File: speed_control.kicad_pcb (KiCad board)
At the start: 2 copper layers, 38.1 x 38.1 mm, 17 parts, among them M1 VAL**, M2 VAL**, M3 VAL**, M4 VAL**, P1 CONN_2, P2 CONN_2, Q1 NPN, SW1 SWITCH_INV, U1 LTC6992_TSOT_32_6

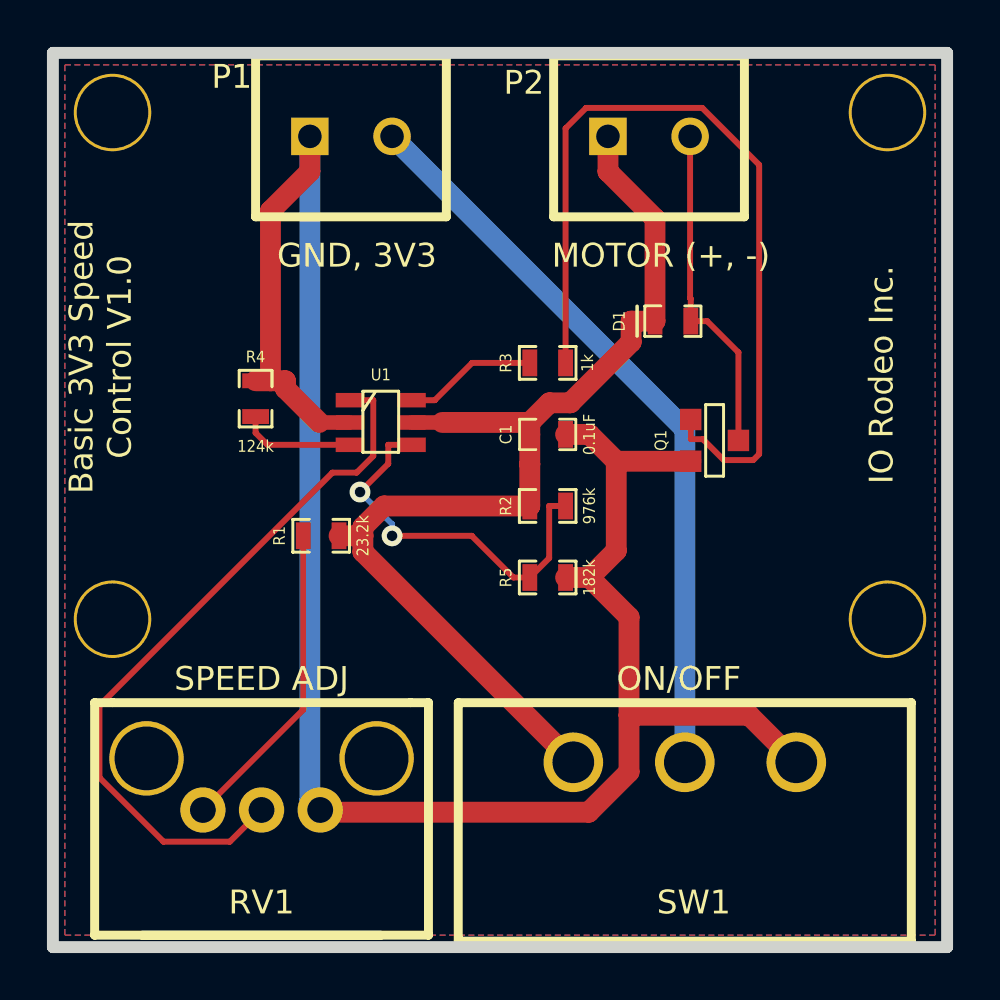
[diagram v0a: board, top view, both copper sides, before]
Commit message: Added trace to PWR class and re-routed. Created gerber files for version 1.1.
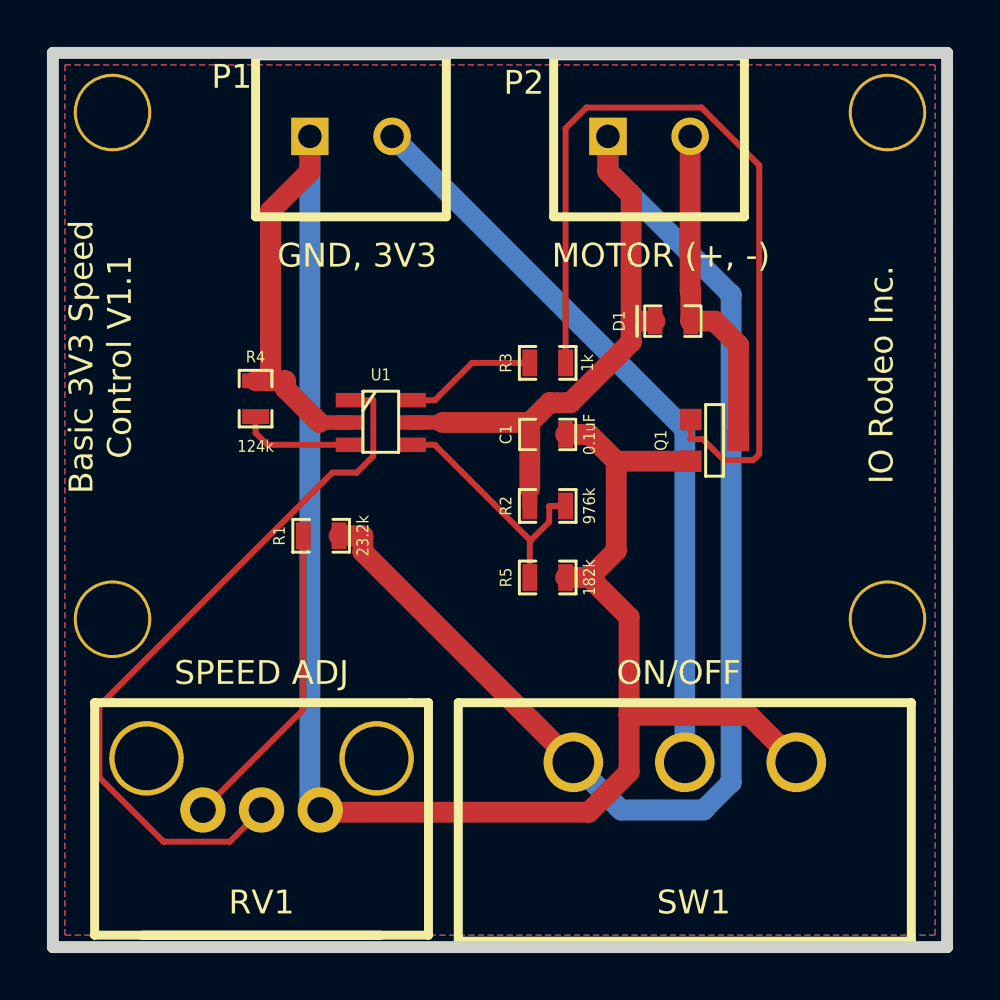
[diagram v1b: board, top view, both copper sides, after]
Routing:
- net +3.3V: track 47.2 -> 76.7 mm
- net N-0000010: track 16.6 -> 10.9 mm, vias 2 -> 0
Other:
- board text added: "Basic 3V3 Speed Control V1.1"
- board text removed: "Basic 3V3 Speed Control V1.0"
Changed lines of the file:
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@@
     (thickness 1.6)
     (drawings 10)
-    (tracks 95)
+    (tracks 90)
     (zones 0)
     (modules 17)
@@
       (drillshape 0)
       (scaleselection 1)
-      (outputdirectory gerber_v1p0/))
+      (outputdirectory gerber_v1p1/))
   )
   (net 0 "")
@@
     (add_net N-000002)
     (add_net N-000003)
-    (add_net N-000004)
     (add_net N-000006)
     (add_net N-000007)
@@
     (add_net GND)
     (add_net N-000001)
+    (add_net N-000004)
   )
   (module SM0603_Capa (layer F.Cu)
@@
     (effects (font (size 1.016 1.016) (thickness 0.2032)))
   )
-  (gr_text "Basic 3V3 Speed \nControl V1.0" (at 27.432 38.354 90) (layer F.SilkS)
+  (gr_text "Basic 3V3 Speed \nControl V1.1" (at 27.432 38.354 90) (layer F.SilkS)
     (effects (font (size 1.016 1.016) (thickness 0.2032)))
   )
-  (gr_text ON/OFF (at 52.07 52.07) (layer F.SilkS)
+  (gr_text ON/OFF (at 52.07 51.816) (layer F.SilkS)
     (effects (font (size 1.016 1.016) (thickness 0.2032)))
   )
-  (gr_text "SPEED ADJ" (at 34.29 52.07) (layer F.SilkS)
+  (gr_text "SPEED ADJ" (at 34.29 51.816) (layer F.SilkS)
     (effects (font (size 1.016 1.016) (thickness 0.2032)))
   )
@@
   (gr_line (start 25.4 63.5) (end 63.5 63.5) (angle 90) (layer Edge.Cuts) (width 0.508))
   (gr_line (start 25.4 25.4) (end 25.4 63.5) (angle 90) (layer Edge.Cuts) (width 0.508))
+  (segment (start 37.592 45.974) (end 38.6083 45.974) (width 0.889) (layer F.Cu) (net 1))
   (segment (start 38.6083 46.6601) (end 38.6083 45.974) (width 0.889) (layer F.Cu) (net 1))
   (segment (start 47.5742 55.626) (end 38.6083 46.6601) (width 0.889) (layer F.Cu) (net 1))
-  (segment (start 37.592 45.974) (end 38.6083 45.974) (width 0.889) (layer F.Cu) (net 1))
-  (segment (start 45.7192 44.704) (end 45.72 44.704) (width 0.6348) (layer F.Cu) (net 1))
-  (segment (start 49.0499 28.956) (end 49.0499 30.4549) (width 0.889) (layer F.Cu) (net 1))
-  (segment (start 39.5078 44.704) (end 45.7192 44.704) (width 0.889) (layer F.Cu) (net 1))
-  (segment (start 38.6083 45.6035) (end 39.5078 44.704) (width 0.889) (layer F.Cu) (net 1))
-  (segment (start 38.6083 45.974) (end 38.6083 45.6035) (width 0.889) (layer F.Cu) (net 1))
-  (segment (start 45.7192 42.9271) (end 45.72 42.9263) (width 0.889) (layer F.Cu) (net 1))
-  (segment (start 45.7192 44.704) (end 45.7192 42.9271) (width 0.889) (layer F.Cu) (net 1))
-  (segment (start 45.72 41.656) (end 45.72 42.9263) (width 0.889) (layer F.Cu) (net 1))
-  (segment (start 51.054 32.459) (end 49.0499 30.4549) (width 0.889) (layer F.Cu) (net 1))
-  (segment (start 51.054 36.83) (end 51.054 32.459) (width 0.889) (layer F.Cu) (net 1))
+  (segment (start 45.72 43.9519) (end 45.72 44.704) (width 0.6348) (layer F.Cu) (net 1))
+  (segment (start 45.72 43.9519) (end 45.72 41.656) (width 0.889) (layer F.Cu) (net 1))
   (segment (start 45.72 41.656) (end 45.72 41.1455) (width 0.889) (layer F.Cu) (net 1))
   (segment (start 41.8567 41.1455) (end 41.8542 41.148) (width 0.6198) (layer F.Cu) (net 1))
   (segment (start 41.989 41.1455) (end 41.8567 41.1455) (width 0.6198) (layer F.Cu) (net 1))
   (segment (start 40.68 41.148) (end 41.8542 41.148) (width 0.6198) (layer F.Cu) (net 1))
+  (segment (start 49.6064 57.6582) (end 47.5742 55.626) (width 0.889) (layer B.Cu) (net 1))
+  (segment (start 53.1243 57.6582) (end 49.6064 57.6582) (width 0.889) (layer B.Cu) (net 1))
+  (segment (start 54.2998 56.4827) (end 53.1243 57.6582) (width 0.889) (layer B.Cu) (net 1))
+  (segment (start 54.2998 35.7048) (end 54.2998 56.4827) (width 0.889) (layer B.Cu) (net 1))
+  (segment (start 49.0499 30.4549) (end 54.2998 35.7048) (width 0.889) (layer B.Cu) (net 1))
+  (segment (start 49.0499 28.956) (end 49.0499 30.4549) (width 0.889) (layer B.Cu) (net 1))
   (segment (start 51.054 36.83) (end 50.0377 36.83) (width 0.889) (layer F.Cu) (net 1))
   (segment (start 45.72 41.1455) (end 41.989 41.1455) (width 0.889) (layer F.Cu) (net 1))
   (segment (start 50.0377 37.7193) (end 50.0377 36.83) (width 0.889) (layer F.Cu) (net 1))
-  (segment (start 47.4476 40.3094) (end 50.0377 37.7193) (width 0.889) (layer F.Cu) (net 1))
-  (segment (start 46.5561 40.3094) (end 47.4476 40.3094) (width 0.889) (layer F.Cu) (net 1))
-  (segment (start 45.72 41.1455) (end 46.5561 40.3094) (width 0.889) (layer F.Cu) (net 1))
+  (segment (start 47.4543 40.3027) (end 50.0377 37.7193) (width 0.889) (layer F.Cu) (net 1))
+  (segment (start 46.5628 40.3027) (end 47.4543 40.3027) (width 0.889) (layer F.Cu) (net 1))
+  (segment (start 45.72 41.1455) (end 46.5628 40.3027) (width 0.889) (layer F.Cu) (net 1))
+  (segment (start 50.0377 31.4427) (end 50.0377 36.83) (width 0.889) (layer F.Cu) (net 1))
+  (segment (start 49.0499 30.4549) (end 50.0377 31.4427) (width 0.889) (layer F.Cu) (net 1))
+  (segment (start 49.0499 28.956) (end 49.0499 30.4549) (width 0.889) (layer F.Cu) (net 1))
   (segment (start 47.244 41.656) (end 48.2603 41.656) (width 0.889) (layer F.Cu) (net 2))
   (segment (start 36.7511 41.148) (end 38.06 41.148) (width 0.6198) (layer F.Cu) (net 2))
@@
   (segment (start 52.324 41.4299) (end 39.8501 28.956) (width 0.889) (layer B.Cu) (net 3))
   (segment (start 52.324 55.626) (end 52.324 41.4299) (width 0.889) (layer B.Cu) (net 3))
-  (via (at 38.4852 44.1096) (size 0.889) (layers F.Cu B.Cu) (net 4))
-  (via (at 39.8521 45.9765) (size 0.889) (layers F.Cu B.Cu) (net 4))
   (segment (start 47.244 44.704) (end 46.5452 44.704) (width 0.254) (layer F.Cu) (net 4))
-  (segment (start 46.5452 46.9268) (end 46.5452 44.704) (width 0.254) (layer F.Cu) (net 4))
-  (segment (start 45.72 47.752) (end 46.5452 46.9268) (width 0.254) (layer F.Cu) (net 4))
-  (segment (start 39.8521 45.4765) (end 38.4852 44.1096) (width 0.254) (layer B.Cu) (net 4))
-  (segment (start 39.8521 45.9765) (end 39.8521 45.4765) (width 0.254) (layer B.Cu) (net 4))
-  (segment (start 39.6887 42.9061) (end 38.4852 44.1096) (width 0.254) (layer F.Cu) (net 4))
-  (segment (start 39.6887 42.098) (end 39.6887 42.9061) (width 0.254) (layer F.Cu) (net 4))
-  (segment (start 43.2457 45.9765) (end 45.0212 47.752) (width 0.254) (layer F.Cu) (net 4))
-  (segment (start 39.8521 45.9765) (end 43.2457 45.9765) (width 0.254) (layer F.Cu) (net 4))
-  (segment (start 45.72 47.752) (end 45.0212 47.752) (width 0.254) (layer F.Cu) (net 4))
-  (segment (start 40.68 42.098) (end 39.6887 42.098) (width 0.254) (layer F.Cu) (net 4))
+  (segment (start 40.68 42.098) (end 41.6713 42.098) (width 0.254) (layer F.Cu) (net 4))
+  (segment (start 41.6713 42.098) (end 45.7521 46.1787) (width 0.254) (layer F.Cu) (net 4))
+  (segment (start 45.72 46.2108) (end 45.7521 46.1787) (width 0.254) (layer F.Cu) (net 4))
+  (segment (start 45.72 47.752) (end 45.72 46.2108) (width 0.254) (layer F.Cu) (net 4))
+  (segment (start 46.5452 45.3856) (end 46.5452 44.704) (width 0.254) (layer F.Cu) (net 4))
+  (segment (start 45.7521 46.1787) (end 46.5452 45.3856) (width 0.254) (layer F.Cu) (net 4))
   (segment (start 53.0975 41.8595) (end 52.578 41.8595) (width 0.254) (layer F.Cu) (net 5))
   (segment (start 53.9866 42.7486) (end 53.0975 41.8595) (width 0.254) (layer F.Cu) (net 5))
-  (segment (start 55.2392 42.7486) (end 53.9866 42.7486) (width 0.254) (layer F.Cu) (net 5))
-  (segment (start 55.492 42.4958) (end 55.2392 42.7486) (width 0.254) (layer F.Cu) (net 5))
-  (segment (start 55.492 30.1687) (end 55.492 42.4958) (width 0.254) (layer F.Cu) (net 5))
-  (segment (start 53.0672 27.7439) (end 55.492 30.1687) (width 0.254) (layer F.Cu) (net 5))
-  (segment (start 48.1173 27.7439) (end 53.0672 27.7439) (width 0.254) (layer F.Cu) (net 5))
-  (segment (start 47.244 28.6172) (end 48.1173 27.7439) (width 0.254) (layer F.Cu) (net 5))
+  (segment (start 55.2434 42.7486) (end 53.9866 42.7486) (width 0.254) (layer F.Cu) (net 5))
+  (segment (start 55.4971 42.4949) (end 55.2434 42.7486) (width 0.254) (layer F.Cu) (net 5))
+  (segment (start 55.4971 30.1916) (end 55.4971 42.4949) (width 0.254) (layer F.Cu) (net 5))
+  (segment (start 53.0324 27.7269) (end 55.4971 30.1916) (width 0.254) (layer F.Cu) (net 5))
+  (segment (start 48.1343 27.7269) (end 53.0324 27.7269) (width 0.254) (layer F.Cu) (net 5))
+  (segment (start 47.244 28.6172) (end 48.1343 27.7269) (width 0.254) (layer F.Cu) (net 5))
   (segment (start 47.244 38.608) (end 47.244 28.6172) (width 0.254) (layer F.Cu) (net 5))
   (segment (start 52.578 41.021) (end 52.578 41.8595) (width 0.254) (layer F.Cu) (net 5))
@@
   (segment (start 41.6713 40.198) (end 43.2613 38.608) (width 0.254) (layer F.Cu) (net 6))
   (segment (start 40.68 40.198) (end 41.6713 40.198) (width 0.254) (layer F.Cu) (net 6))
-  (segment (start 52.5501 35.8493) (end 52.578 35.8772) (width 0.254) (layer F.Cu) (net 7))
-  (segment (start 52.5501 28.956) (end 52.5501 35.8493) (width 0.254) (layer F.Cu) (net 7))
-  (segment (start 52.578 36.83) (end 52.578 35.8772) (width 0.254) (layer F.Cu) (net 7))
-  (segment (start 54.61 38.1632) (end 53.2768 36.83) (width 0.254) (layer F.Cu) (net 7))
-  (segment (start 54.61 41.91) (end 54.61 38.1632) (width 0.254) (layer F.Cu) (net 7))
-  (segment (start 52.578 36.83) (end 53.2768 36.83) (width 0.254) (layer F.Cu) (net 7))
+  (segment (start 54.61 37.8457) (end 53.5943 36.83) (width 0.889) (layer F.Cu) (net 7))
+  (segment (start 54.61 41.91) (end 54.61 37.8457) (width 0.889) (layer F.Cu) (net 7))
+  (segment (start 52.578 36.83) (end 53.5943 36.83) (width 0.889) (layer F.Cu) (net 7))
+  (segment (start 52.5501 35.5318) (end 52.578 35.5597) (width 0.889) (layer F.Cu) (net 7))
+  (segment (start 52.5501 28.956) (end 52.5501 35.5318) (width 0.889) (layer F.Cu) (net 7))
+  (segment (start 52.578 36.83) (end 52.578 35.5597) (width 0.889) (layer F.Cu) (net 7))
   (segment (start 34.5412 42.098) (end 34.036 41.5928) (width 0.254) (layer F.Cu) (net 8))
   (segment (start 38.06 42.098) (end 34.5412 42.098) (width 0.254) (layer F.Cu) (net 8))

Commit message: Flipped potentiometer so direction of rotation is typical (as opposed to reverse). Added indicator LED. Re-routed.
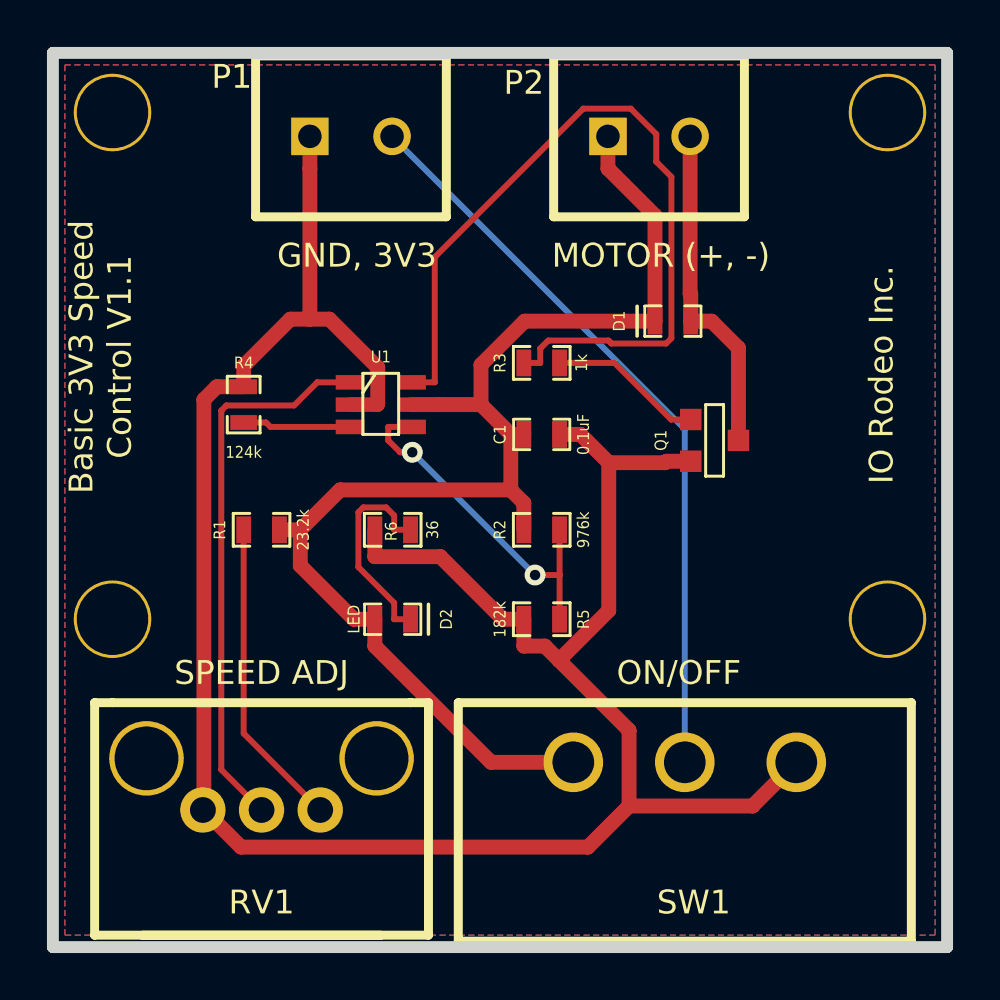
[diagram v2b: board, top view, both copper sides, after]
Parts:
- added D2: LED, SM0603_Diode, F.Cu at (39.9, 49.5)
- added R6: 36, SM0603_Resistor, F.Cu at (39.9, 45.7)
- moved R1 2.55 mm to (34.3, 45.7)
- moved R5 1.80 mm to (46.2, 49.5), turned to 180 degrees
- moved R2 1.05 mm to (46.2, 45.7)
- moved U1 0.76 mm to (39.4, 40.4)
- moved R4 0.57 mm to (33.5, 40.4)
- moved C1 0.25 mm to (46.2, 41.7)
- moved R3 0.25 mm to (46.2, 38.6)
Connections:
- R1 pad 2: N-000007 (its old number) -> N-000008
- RV1 pad 1: N-000007 (its old number) -> GND
- RV1 pad 3: GND -> N-000008
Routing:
- net N-000003: track 36.2 -> 6.59 mm
- net N-000009: track 5.70 -> 35.0 mm
- net +3.3V: track 76.7 -> 56.1 mm
- net N-000007 (its old number): track 13.5 -> 0.00 mm
- net N-000008: track 0.00 -> 13.3 mm
- net GND: track 88.0 -> 100.0 mm
- net N-000005: track 0.00 -> 8.95 mm
- net N-000006: track 31.1 -> 23.7 mm
- net N-0000011: track 10.9 -> 15.1 mm, vias 0 -> 2
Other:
- net class PWR: trace_width 0.889 -> 0.635
